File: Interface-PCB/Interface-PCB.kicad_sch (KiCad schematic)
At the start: 16 parts, among them J1 BARREL_JACK_PAD, J2 BARREL_JACK_PAD, J3 GPIO_DEBUG_HEADER, J4 RASPBERRYPI_GPIO_CONN_HEADER, M1 PERISTALTIC_PUMP, M2 PERISTALTIC_PUMP, M3 PERISTALTIC_PUMP, U1 TB6612FNG_BREAKOUT, U2 TB6612FNG_BREAKOUT

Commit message: Increase board size, Add connector labels
- Increase board size to 140x130mm
- Refine layout on PCB
- Align breakout board resistors to 2.54mm spacing
- Add Inverted silkscreen labels for off-board connectors
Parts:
- J1, J2, M1, M2, M3: footprint AA_Custom_Components:PowerPad_Pair_4.0x4.0mm -> AA_Custom_Components:PowerPad_Pair_5.0x5.0mm
- TP1, TP2, TP3: footprint AA_Custom_Components:TestPoint_Pad_4.0x4.0mm -> AA_Custom_Components:TestPoint_Pad_5.0x5.0mm
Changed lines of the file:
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@@
       (effects (font (size 1.143 1.143)))
     )
-    (property "Footprint" "AA_Custom_Components:PowerPad_Pair_4.0x4.0mm" (id 2) (at 30.48 157.48 0)
+    (property "Footprint" "AA_Custom_Components:PowerPad_Pair_5.0x5.0mm" (id 2) (at 30.48 157.48 0)
       (effects (font (size 0.508 0.508)) hide)
     )
@@
       (effects (font (size 1.143 1.143)))
     )
-    (property "Footprint" "AA_Custom_Components:PowerPad_Pair_4.0x4.0mm" (id 2) (at 30.48 176.53 0)
+    (property "Footprint" "AA_Custom_Components:PowerPad_Pair_5.0x5.0mm" (id 2) (at 30.48 176.53 0)
       (effects (font (size 0.508 0.508)) hide)
     )
@@
       (effects (font (size 1.143 1.143)))
     )
-    (property "Footprint" "AA_Custom_Components:PowerPad_Pair_4.0x4.0mm" (id 2) (at 105.41 157.48 0)
+    (property "Footprint" "AA_Custom_Components:PowerPad_Pair_5.0x5.0mm" (id 2) (at 105.41 157.48 0)
       (effects (font (size 0.508 0.508)) hide)
     )
@@
     (property "Reference" "J1" (id 0) (at 30.6578 60.325 0))
     (property "Value" "BARREL_JACK_PAD" (id 1) (at 30.6578 62.6364 0))
-    (property "Footprint" "AA_Custom_Components:PowerPad_Pair_4.0x4.0mm" (id 2) (at 30.48 69.596 0)
+    (property "Footprint" "AA_Custom_Components:PowerPad_Pair_5.0x5.0mm" (id 2) (at 30.48 69.596 0)
       (effects (font (size 1.27 1.27)) hide)
     )
@@
     (property "Reference" "J2" (id 0) (at 31.9278 86.995 0))
     (property "Value" "BARREL_JACK_PAD" (id 1) (at 31.9278 89.3064 0))
-    (property "Footprint" "AA_Custom_Components:PowerPad_Pair_4.0x4.0mm" (id 2) (at 31.75 96.266 0)
+    (property "Footprint" "AA_Custom_Components:PowerPad_Pair_5.0x5.0mm" (id 2) (at 31.75 96.266 0)
       (effects (font (size 1.27 1.27)) hide)
     )
@@
       (effects (font (size 1.27 1.27)) (justify left))
     )
-    (property "Footprint" "AA_Custom_Components:TestPoint_Pad_4.0x4.0mm" (id 2) (at 256.54 153.67 0)
+    (property "Footprint" "AA_Custom_Components:TestPoint_Pad_5.0x5.0mm" (id 2) (at 256.54 153.67 0)
       (effects (font (size 1.27 1.27)) hide)
     )
@@
       (effects (font (size 1.27 1.27)) (justify left))
     )
-    (property "Footprint" "AA_Custom_Components:TestPoint_Pad_4.0x4.0mm" (id 2) (at 243.84 153.67 0)
+    (property "Footprint" "AA_Custom_Components:TestPoint_Pad_5.0x5.0mm" (id 2) (at 243.84 153.67 0)
       (effects (font (size 1.27 1.27)) hide)
     )
@@
       (effects (font (size 1.27 1.27)) (justify left))
     )
-    (property "Footprint" "AA_Custom_Components:TestPoint_Pad_4.0x4.0mm" (id 2) (at 231.14 154.94 0)
+    (property "Footprint" "AA_Custom_Components:TestPoint_Pad_5.0x5.0mm" (id 2) (at 231.14 154.94 0)
       (effects (font (size 1.27 1.27)) hide)
     )
@@
     )
     (path "/00000000-0000-0000-0000-000063af14b6"
-      (reference "J1") (unit 1) (value "BARREL_JACK_PAD") (footprint "AA_Custom_Components:PowerPad_Pair_4.0x4.0mm")
+      (reference "J1") (unit 1) (value "BARREL_JACK_PAD") (footprint "AA_Custom_Components:PowerPad_Pair_5.0x5.0mm")
     )
     (path "/00000000-0000-0000-0000-000063b7d3d0"
-      (reference "J2") (unit 1) (value "BARREL_JACK_PAD") (footprint "AA_Custom_Components:PowerPad_Pair_4.0x4.0mm")
+      (reference "J2") (unit 1) (value "BARREL_JACK_PAD") (footprint "AA_Custom_Components:PowerPad_Pair_5.0x5.0mm")
     )
     (path "/00000000-0000-0000-0000-000063ceadab"
@@
     )
     (path "/00000000-0000-0000-0000-0000638d58ae"
-      (reference "M1") (unit 1) (value "PERISTALTIC_PUMP") (footprint "AA_Custom_Components:PowerPad_Pair_4.0x4.0mm")
+      (reference "M1") (unit 1) (value "PERISTALTIC_PUMP") (footprint "AA_Custom_Components:PowerPad_Pair_5.0x5.0mm")
     )
     (path "/00000000-0000-0000-0000-0000639395b5"
-      (reference "M2") (unit 1) (value "PERISTALTIC_PUMP") (footprint "AA_Custom_Components:PowerPad_Pair_4.0x4.0mm")
+      (reference "M2") (unit 1) (value "PERISTALTIC_PUMP") (footprint "AA_Custom_Components:PowerPad_Pair_5.0x5.0mm")
     )
     (path "/00000000-0000-0000-0000-000063a48f2d"
-      (reference "M3") (unit 1) (value "PERISTALTIC_PUMP") (footprint "AA_Custom_Components:PowerPad_Pair_4.0x4.0mm")
+      (reference "M3") (unit 1) (value "PERISTALTIC_PUMP") (footprint "AA_Custom_Components:PowerPad_Pair_5.0x5.0mm")
     )
     (path "/00000000-0000-0000-0000-00006375997b/00000000-0000-0000-0000-000063bd2f18"
@@
     )
     (path "/b587b45d-477b-43d3-b805-5d3475a6e5e8"
-      (reference "TP1") (unit 1) (value "GND_PAD") (footprint "AA_Custom_Components:TestPoint_Pad_4.0x4.0mm")
+      (reference "TP1") (unit 1) (value "GND_PAD") (footprint "AA_Custom_Components:TestPoint_Pad_5.0x5.0mm")
     )
     (path "/9ba1cdc8-1a44-45d8-af29-47fd8c45aa17"
-      (reference "TP2") (unit 1) (value "5V_PAD") (footprint "AA_Custom_Components:TestPoint_Pad_4.0x4.0mm")
+      (reference "TP2") (unit 1) (value "5V_PAD") (footprint "AA_Custom_Components:TestPoint_Pad_5.0x5.0mm")
     )
     (path "/949f8304-cb62-4014-8dc3-9146e947ad99"
-      (reference "TP3") (unit 1) (value "3.3V_PAD") (footprint "AA_Custom_Components:TestPoint_Pad_4.0x4.0mm")
+      (reference "TP3") (unit 1) (value "3.3V_PAD") (footprint "AA_Custom_Components:TestPoint_Pad_5.0x5.0mm")
     )
     (path "/00000000-0000-0000-0000-00006375997b/623e802f-a925-4434-8a77-c99f007adf0f"

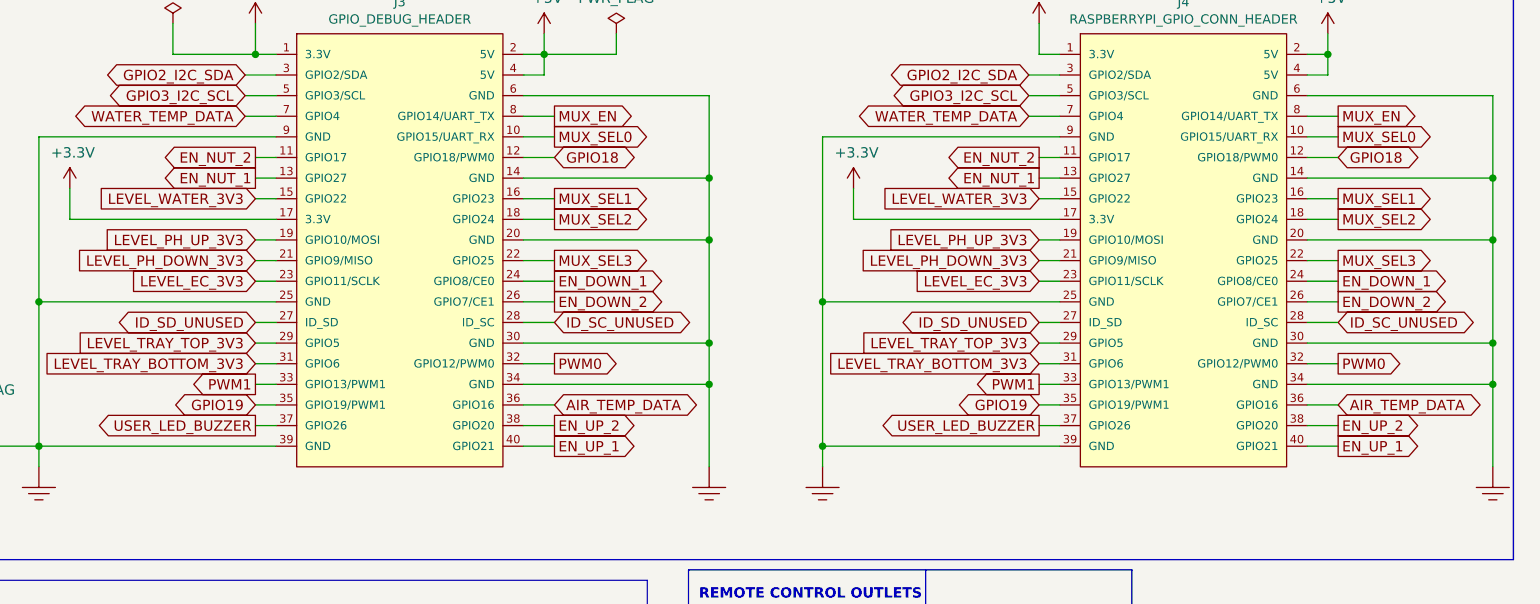
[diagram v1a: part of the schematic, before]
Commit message: Create ground plane, swap motor driver pins
- Create Ground pour/plane on F.Copper
- Swap motor driver pin assignments, to resolve some route
  criss-crossing
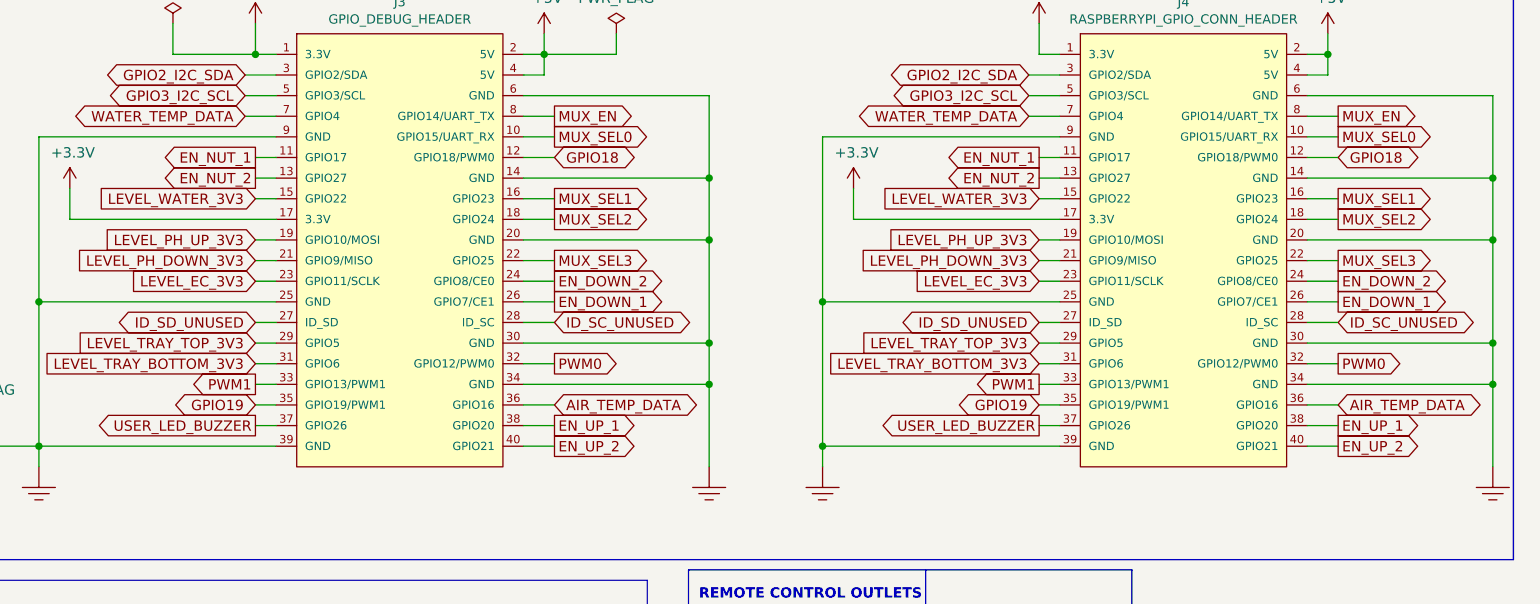
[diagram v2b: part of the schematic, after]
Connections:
- net EN_DOWN_1: now also J3.26 (GPIO7/CE1), J4.26 (GPIO7/CE1); no longer J3.24 (GPIO8/CE0), J4.24 (GPIO8/CE0)
- net EN_DOWN_2: now also J3.24 (GPIO8/CE0), J4.24 (GPIO8/CE0); no longer J3.26 (GPIO7/CE1), J4.26 (GPIO7/CE1)
- net EN_NUT_1: now also J3.11 (GPIO17), J4.11 (GPIO17); no longer J3.13 (GPIO27), J4.13 (GPIO27)
- net EN_NUT_2: now also J3.13 (GPIO27), J4.13 (GPIO27); no longer J3.11 (GPIO17), J4.11 (GPIO17)
- net EN_UP_1: now also J3.38 (GPIO20), J4.38 (GPIO20); no longer J3.40 (GPIO21), J4.40 (GPIO21)
- net EN_UP_2: now also J3.40 (GPIO21), J4.40 (GPIO21); no longer J3.38 (GPIO20), J4.38 (GPIO20)
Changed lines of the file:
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@@
     )
   )
-  (global_label "EN_DOWN_2" (shape output) (at 242.57 99.06 0) (fields_autoplaced)
-    (effects (font (size 1.27 1.27)) (justify left))
-    (property "Intersheet References" "${INTERSHEET_REFS}" (id 0) (at 0 0 0)
+  (global_label "EN_DOWN_2" (shape output) (at 242.57 96.52 0) (fields_autoplaced)
+    (effects (font (size 1.27 1.27)) (justify left))
+    (property "Intersheet References" "${INTERSHEET_REFS}" (id 0) (at 0 -2.54 0)
       (effects (font (size 1.27 1.27)) hide)
     )
@@
     )
   )
-  (global_label "EN_NUT_2" (shape output) (at 205.74 81.28 180) (fields_autoplaced)
-    (effects (font (size 1.27 1.27)) (justify right))
-    (property "Intersheet References" "${INTERSHEET_REFS}" (id 0) (at 0 0 0)
-      (effects (font (size 1.27 1.27)) hide)
-    )
-  )
   (global_label "ID_SC_UNUSED" (shape bidirectional) (at 146.05 101.6 0) (fields_autoplaced)
     (effects (font (size 1.27 1.27)) (justify left))
@@
     )
   )
+  (global_label "EN_DOWN_1" (shape output) (at 146.05 99.06 0) (fields_autoplaced)
+    (effects (font (size 1.27 1.27)) (justify left))
+    (property "Intersheet References" "${INTERSHEET_REFS}" (id 0) (at -96.52 2.54 0)
+      (effects (font (size 1.27 1.27)) hide)
+    )
+  )
   (global_label "EN_UP_2" (shape input) (at 72.39 158.75 0) (fields_autoplaced)
     (effects (font (size 1.27 1.27)) (justify left))
@@
     )
   )
-  (global_label "EN_DOWN_1" (shape output) (at 146.05 96.52 0) (fields_autoplaced)
-    (effects (font (size 1.27 1.27)) (justify left))
-    (property "Intersheet References" "${INTERSHEET_REFS}" (id 0) (at 0 0 0)
-      (effects (font (size 1.27 1.27)) hide)
-    )
-  )
   (global_label "LEVEL_TRAY_BOTTOM_3V3" (shape input) (at 109.22 106.68 180) (fields_autoplaced)
     (effects (font (size 1.27 1.27)) (justify right))
@@
     )
   )
+  (global_label "EN_UP_1" (shape output) (at 146.05 114.3 0) (fields_autoplaced)
+    (effects (font (size 1.27 1.27)) (justify left))
+    (property "Intersheet References" "${INTERSHEET_REFS}" (id 0) (at 0 -2.54 0)
+      (effects (font (size 1.27 1.27)) hide)
+    )
+  )
   (global_label "GPIO19" (shape bidirectional) (at 109.22 111.76 180) (fields_autoplaced)
     (effects (font (size 1.27 1.27)) (justify right))
@@
     )
   )
-  (global_label "EN_UP_2" (shape output) (at 146.05 114.3 0) (fields_autoplaced)
-    (effects (font (size 1.27 1.27)) (justify left))
-    (property "Intersheet References" "${INTERSHEET_REFS}" (id 0) (at 0 0 0)
+  (global_label "EN_UP_2" (shape output) (at 146.05 116.84 0) (fields_autoplaced)
+    (effects (font (size 1.27 1.27)) (justify left))
+    (property "Intersheet References" "${INTERSHEET_REFS}" (id 0) (at 0 2.54 0)
       (effects (font (size 1.27 1.27)) hide)
     )
@@
     )
   )
-  (global_label "EN_UP_1" (shape output) (at 146.05 116.84 0) (fields_autoplaced)
-    (effects (font (size 1.27 1.27)) (justify left))
-    (property "Intersheet References" "${INTERSHEET_REFS}" (id 0) (at 0 0 0)
-      (effects (font (size 1.27 1.27)) hide)
-    )
-  )
   (global_label "MUX_SEL2" (shape output) (at 146.05 88.9 0) (fields_autoplaced)
     (effects (font (size 1.27 1.27)) (justify left))
@@
     )
   )
-  (global_label "EN_DOWN_1" (shape output) (at 242.57 96.52 0) (fields_autoplaced)
-    (effects (font (size 1.27 1.27)) (justify left))
-    (property "Intersheet References" "${INTERSHEET_REFS}" (id 0) (at 0 0 0)
-      (effects (font (size 1.27 1.27)) hide)
-    )
-  )
-  (global_label "EN_DOWN_2" (shape output) (at 146.05 99.06 0) (fields_autoplaced)
-    (effects (font (size 1.27 1.27)) (justify left))
-    (property "Intersheet References" "${INTERSHEET_REFS}" (id 0) (at 0 0 0)
+  (global_label "EN_DOWN_1" (shape output) (at 242.57 99.06 0) (fields_autoplaced)
+    (effects (font (size 1.27 1.27)) (justify left))
+    (property "Intersheet References" "${INTERSHEET_REFS}" (id 0) (at 0 2.54 0)
+      (effects (font (size 1.27 1.27)) hide)
+    )
+  )
+  (global_label "EN_DOWN_2" (shape output) (at 146.05 96.52 0) (fields_autoplaced)
+    (effects (font (size 1.27 1.27)) (justify left))
+    (property "Intersheet References" "${INTERSHEET_REFS}" (id 0) (at -96.52 -2.54 0)
       (effects (font (size 1.27 1.27)) hide)
     )
@@
     (effects (font (size 1.27 1.27)) (justify right))
     (property "Intersheet References" "${INTERSHEET_REFS}" (id 0) (at 0 0 0)
+      (effects (font (size 1.27 1.27)) hide)
+    )
+  )
+  (global_label "EN_NUT_1" (shape output) (at 205.74 81.28 180) (fields_autoplaced)
+    (effects (font (size 1.27 1.27)) (justify right))
+    (property "Intersheet References" "${INTERSHEET_REFS}" (id 0) (at 96.52 -2.54 0)
       (effects (font (size 1.27 1.27)) hide)
     )
@@
     )
   )
-  (global_label "EN_UP_1" (shape output) (at 242.57 116.84 0) (fields_autoplaced)
-    (effects (font (size 1.27 1.27)) (justify left))
-    (property "Intersheet References" "${INTERSHEET_REFS}" (id 0) (at 0 0 0)
-      (effects (font (size 1.27 1.27)) hide)
-    )
-  )
-  (global_label "EN_UP_2" (shape output) (at 242.57 114.3 0) (fields_autoplaced)
-    (effects (font (size 1.27 1.27)) (justify left))
-    (property "Intersheet References" "${INTERSHEET_REFS}" (id 0) (at 0 0 0)
+  (global_label "EN_UP_1" (shape output) (at 242.57 114.3 0) (fields_autoplaced)
+    (effects (font (size 1.27 1.27)) (justify left))
+    (property "Intersheet References" "${INTERSHEET_REFS}" (id 0) (at 0 -2.54 0)
+      (effects (font (size 1.27 1.27)) hide)
+    )
+  )
+  (global_label "EN_NUT_2" (shape output) (at 205.74 83.82 180) (fields_autoplaced)
+    (effects (font (size 1.27 1.27)) (justify right))
+    (property "Intersheet References" "${INTERSHEET_REFS}" (id 0) (at 96.52 2.54 0)
+      (effects (font (size 1.27 1.27)) hide)
+    )
+  )
+  (global_label "EN_UP_2" (shape output) (at 242.57 116.84 0) (fields_autoplaced)
+    (effects (font (size 1.27 1.27)) (justify left))
+    (property "Intersheet References" "${INTERSHEET_REFS}" (id 0) (at 0 2.54 0)
       (effects (font (size 1.27 1.27)) hide)
     )
@@
     )
   )
-  (global_label "EN_NUT_2" (shape output) (at 109.22 81.28 180) (fields_autoplaced)
-    (effects (font (size 1.27 1.27)) (justify right))
-    (property "Intersheet References" "${INTERSHEET_REFS}" (id 0) (at 0 0 0)
+  (global_label "EN_NUT_2" (shape output) (at 109.22 83.82 180) (fields_autoplaced)
+    (effects (font (size 1.27 1.27)) (justify right))
+    (property "Intersheet References" "${INTERSHEET_REFS}" (id 0) (at 0 2.54 0)
       (effects (font (size 1.27 1.27)) hide)
     )
@@
     )
   )
-  (global_label "EN_NUT_1" (shape output) (at 205.74 83.82 180) (fields_autoplaced)
-    (effects (font (size 1.27 1.27)) (justify right))
-    (property "Intersheet References" "${INTERSHEET_REFS}" (id 0) (at 0 0 0)
-      (effects (font (size 1.27 1.27)) hide)
-    )
-  )
   (global_label "ID_SC_UNUSED" (shape bidirectional) (at 242.57 101.6 0) (fields_autoplaced)
     (effects (font (size 1.27 1.27)) (justify left))
@@
     )
   )
-  (global_label "EN_NUT_1" (shape output) (at 109.22 83.82 180) (fields_autoplaced)
-    (effects (font (size 1.27 1.27)) (justify right))
-    (property "Intersheet References" "${INTERSHEET_REFS}" (id 0) (at 0 0 0)
-      (effects (font (size 1.27 1.27)) hide)
-    )
+  (global_label "EN_NUT_1" (shape output) (at 109.22 81.28 180) (fields_autoplaced)
+    (effects (font (size 1.27 1.27)) (justify right))
+    (property "Intersheet References" "${INTERSHEET_REFS}" (id 0) (at 0 -2.54 0)
+      (effects (font (size 1.27 1.27)) hide)
+    )
